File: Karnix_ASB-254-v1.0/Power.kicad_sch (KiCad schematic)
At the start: 37 parts, among them Q1 AO3401A, U1 ST1S14, U2 TLV62565DBVT, U3 RS3236-2.5YF5, U4 RS3236-3.3YF5

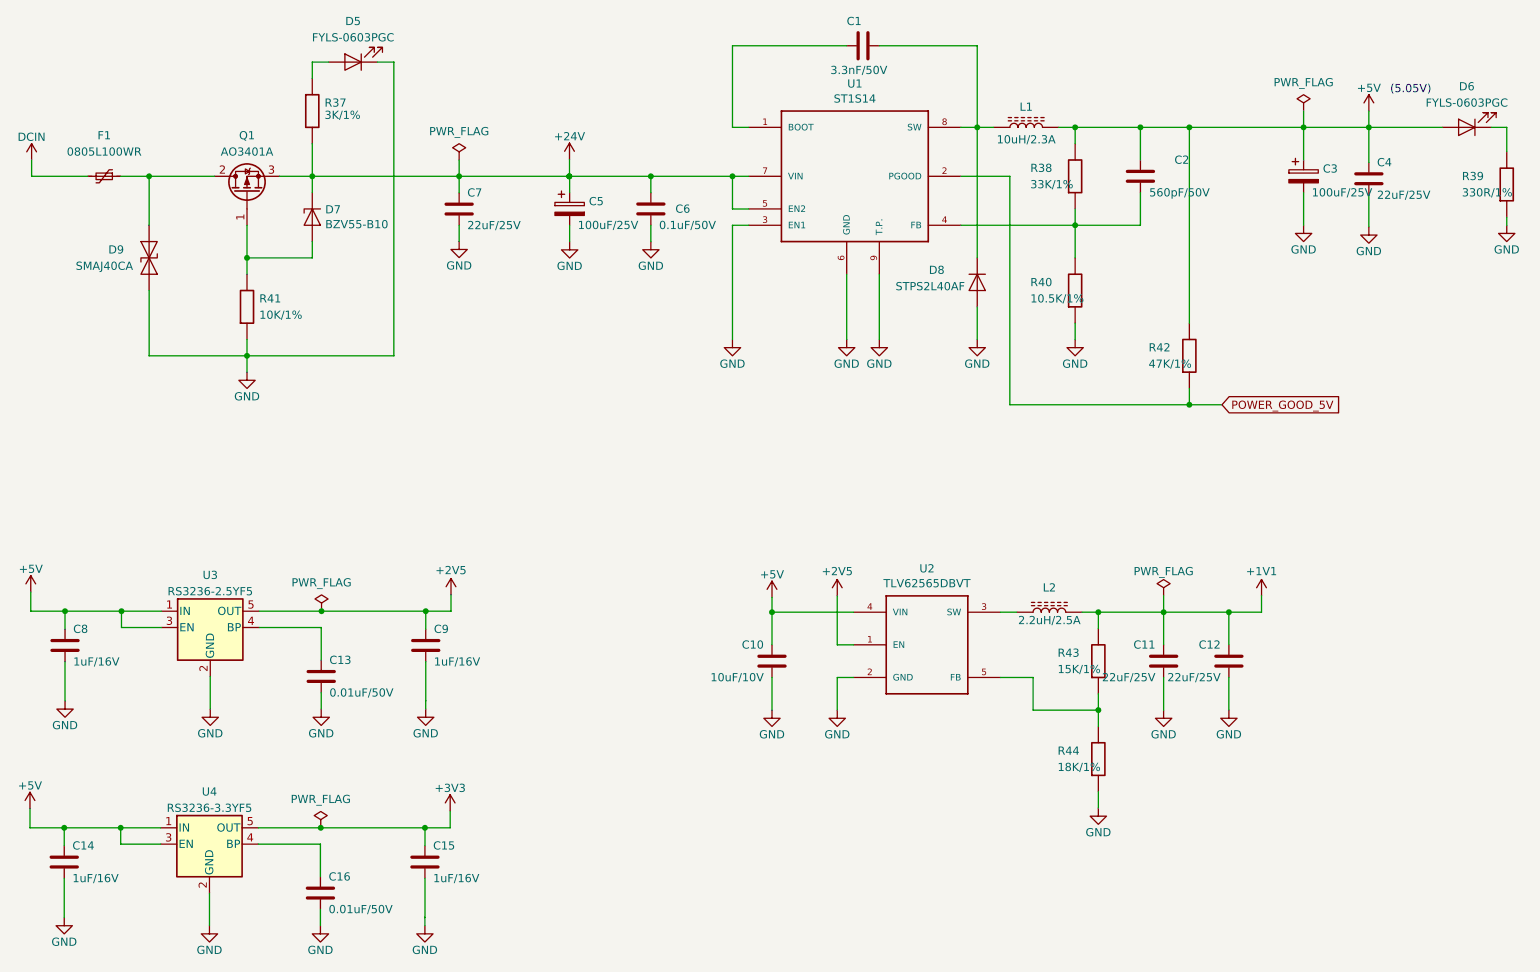
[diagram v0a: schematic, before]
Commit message: Optimize component base
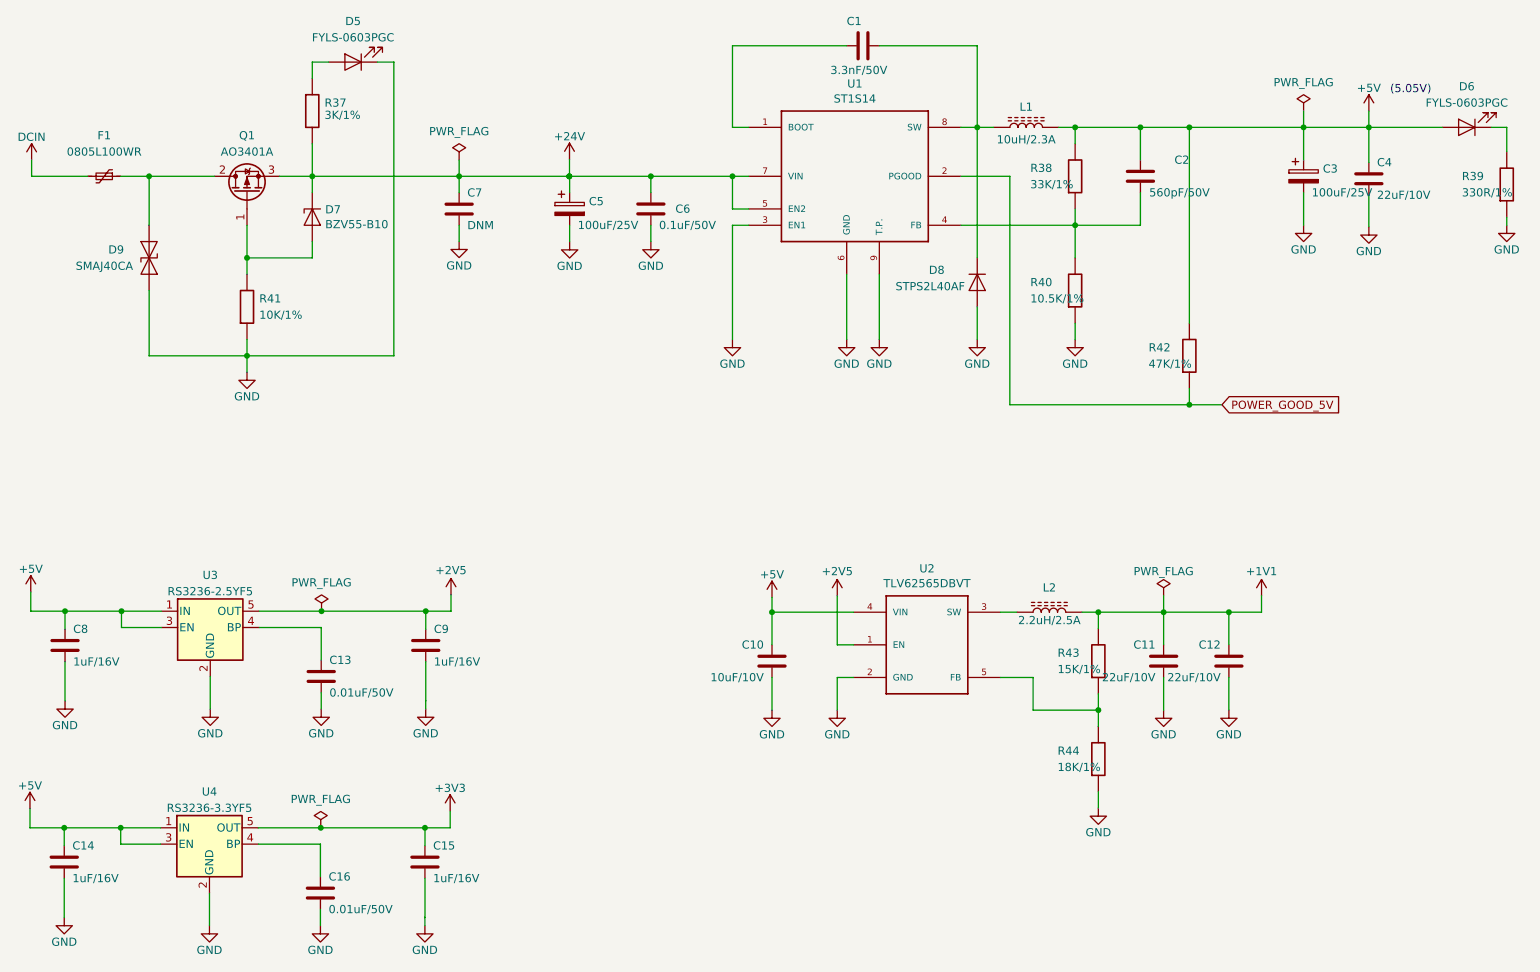
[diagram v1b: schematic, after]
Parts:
- C11, C12: value 22uF/25V -> 22uF/10V; Mfr. Part Number GRT21BR61E226ME13L -> TCC0805X5R226M100FT
- C4: value 22uF/25V -> 22uF/10V; Mfr. Part Number C2220C226J3RACTU -> TCC0805X5R226M100FT
- C6: footprint Fabmicro:C_0402_1005Metric -> Capacitor_SMD:C_0402_1005Metric
- C7: value 22uF/25V -> DNM; Mfr. Part Number C2220C226J3RACTU -> (none)
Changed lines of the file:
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@@
   (title_block
     (title "ПИР СЦХ-254 \"Карно\"\n(Karnix ASB-254)")
-    (date "2023-10-20")
+    (date "2023-10-21")
     (rev "V1.0")
     (company "ООО \"Фабмикро\"")
@@
       (effects (font (size 1.27 1.27)) (justify left))
     )
-    (property "Value" "22uF/25V" (at 268.7882 139.7322 90)
+    (property "Value" "22uF/10V" (at 268.7882 139.7322 90)
       (effects (font (size 1.27 1.27)) (justify left))
     )
@@
       (effects (font (size 1.27 1.27)) hide)
     )
-    (property "Mfr. Part Number" "GRT21BR61E226ME13L" (at 270.0582 137.1922 0)
+    (property "Mfr. Part Number" "TCC0805X5R226M100FT" (at 270.0582 137.1922 0)
       (effects (font (size 1.27 1.27)) hide)
     )
@@
       (effects (font (size 1.27 1.27)) (justify left))
     )
-    (property "Value" "22uF/25V" (at 278.9482 139.7322 90)
+    (property "Value" "22uF/10V" (at 278.9482 139.7322 90)
       (effects (font (size 1.27 1.27)) (justify left))
     )
@@
       (effects (font (size 1.27 1.27)) hide)
     )
-    (property "Mfr. Part Number" "GRT21BR61E226ME13L" (at 280.2182 137.1922 0)
+    (property "Mfr. Part Number" "TCC0805X5R226M100FT" (at 280.2182 137.1922 0)
       (effects (font (size 1.27 1.27)) hide)
     )
@@
       (effects (font (size 1.27 1.27)) (justify left))
     )
-    (property "Value" "22uF/25V" (at 161.671 69.3616 90)
+    (property "Value" "DNM" (at 161.671 69.3616 90)
       (effects (font (size 1.27 1.27)) (justify left))
     )
@@
       (effects (font (size 1.27 1.27)) hide)
     )
-    (property "Mfr. Part Number" "C2220C226J3RACTU" (at 160.401 66.8216 0)
+    (property "Mfr. Part Number" "" (at 160.401 66.8216 0)
       (effects (font (size 1.27 1.27)) hide)
     )
@@
       (effects (font (size 1.27 1.27)) (justify left))
     )
-    (property "Value" "22uF/25V" (at 303.276 64.643 90)
+    (property "Value" "22uF/10V" (at 303.276 64.643 90)
       (effects (font (size 1.27 1.27)) (justify left))
     )
@@
       (effects (font (size 1.27 1.27)) hide)
     )
-    (property "Mfr. Part Number" "C2220C226J3RACTU" (at 302.006 62.103 0)
+    (property "Mfr. Part Number" "TCC0805X5R226M100FT" (at 302.006 62.103 0)
       (effects (font (size 1.27 1.27)) hide)
     )
@@
       (effects (font (size 1.27 1.27)) (justify left))
     )
-    (property "Footprint" "Fabmicro:C_0402_1005Metric" (at 191.2112 70.612 90)
-      (effects (font (size 1.27 1.27)) hide)
-    )
+    (property "Footprint" "Capacitor_SMD:C_0402_1005Metric" (at 191.2112 70.612 90)
+      (effects (font (size 1.27 1.27)) hide)
+    )
